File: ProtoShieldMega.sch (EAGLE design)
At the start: 32 parts, among them J1 Digital_0_7, J2 Analog, J3 Digital_8_13, J4 Analog, J5 Digital_0_7, J6 Digital_22_36, J7 Digital_23_37, J8 Digital_38_52, J9 Digital_39_53

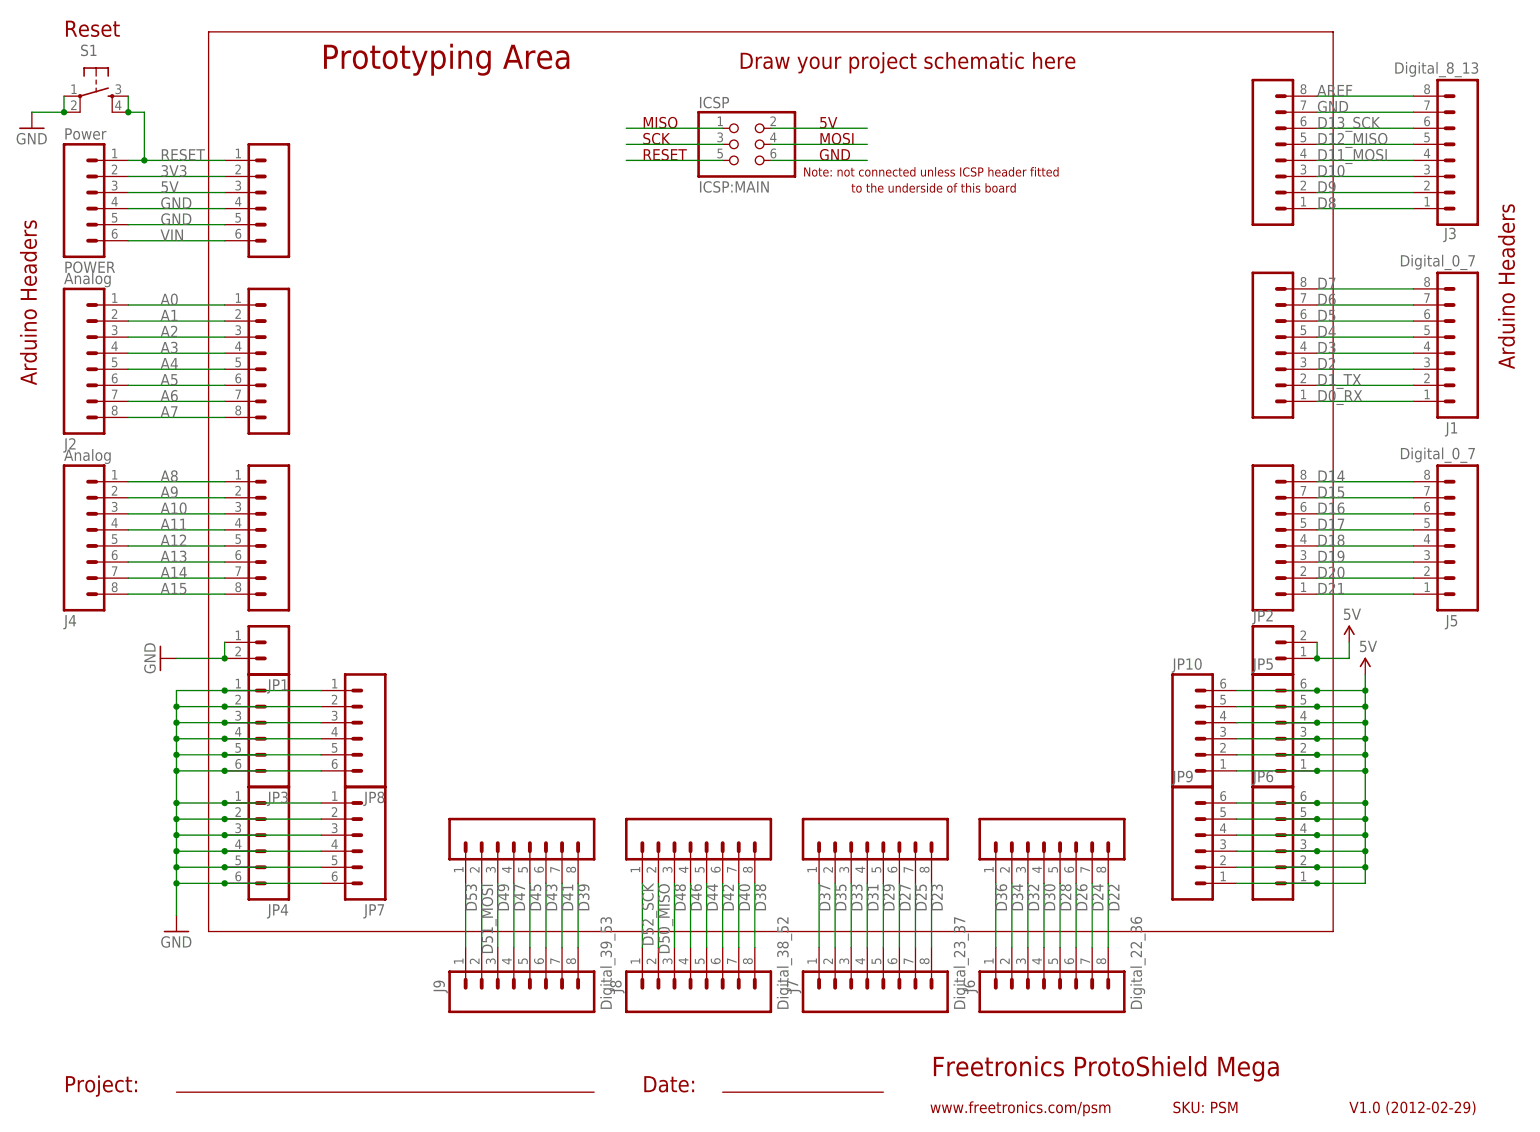
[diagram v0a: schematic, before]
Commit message: Update for Arduino R3 headers
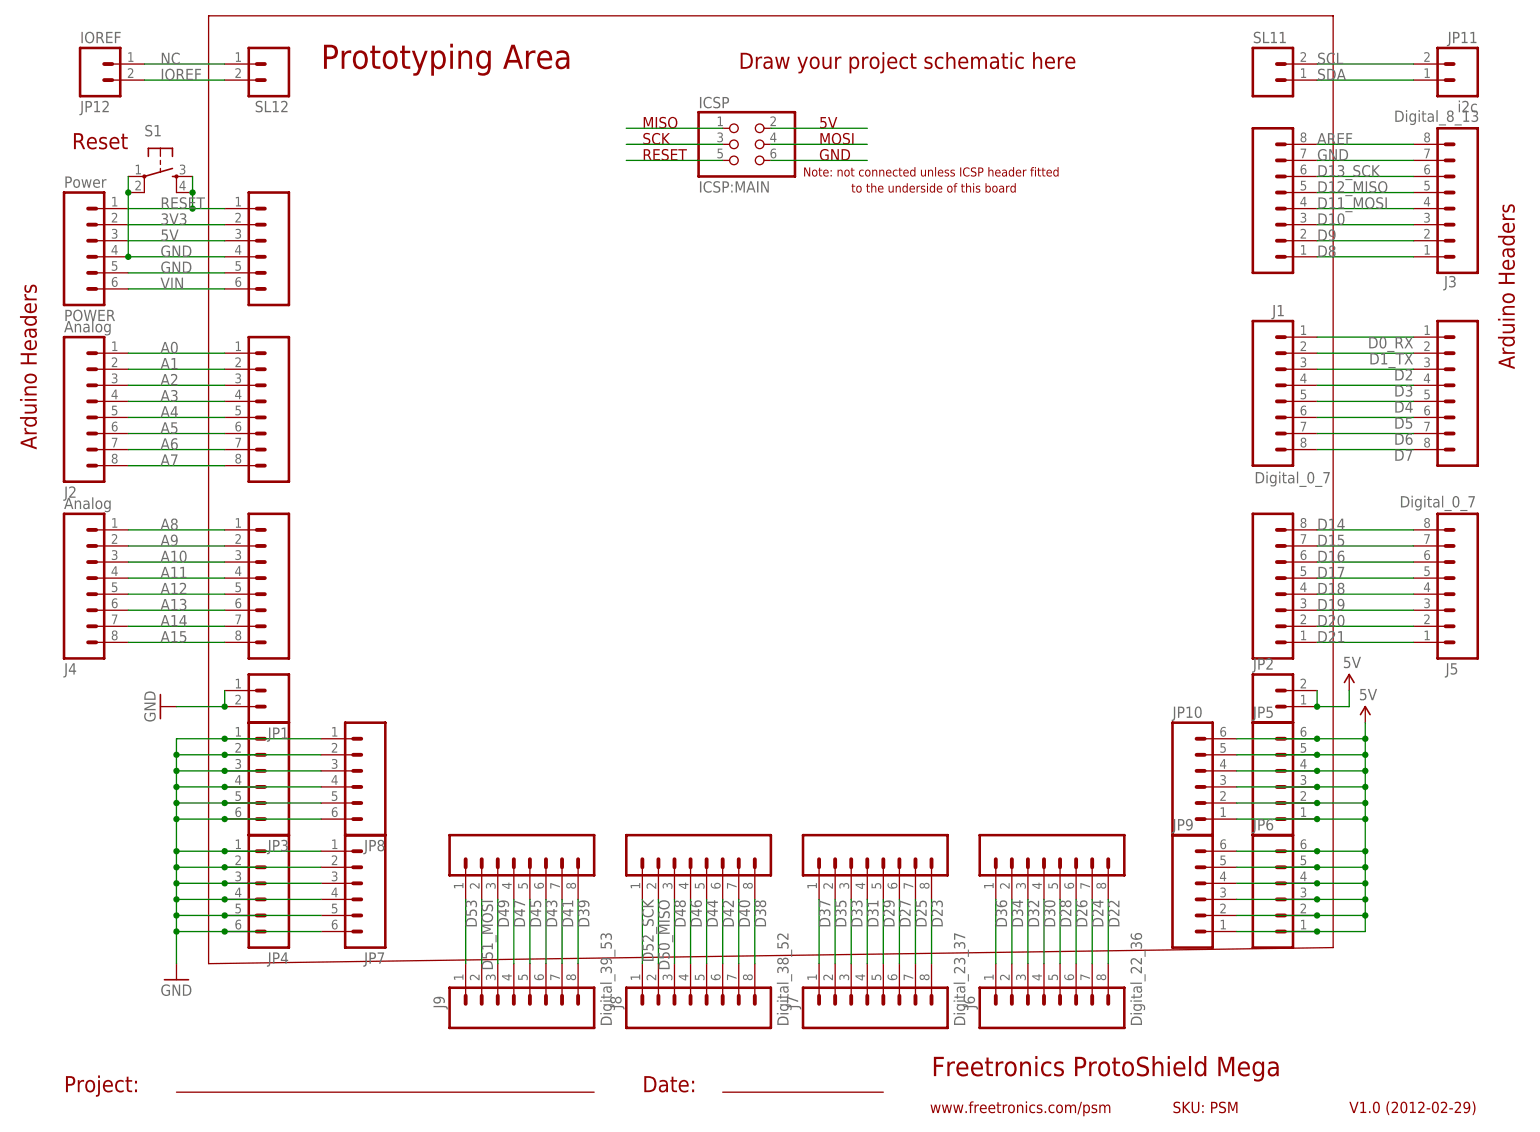
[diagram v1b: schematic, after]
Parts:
- added JP11: i2c, freetronics:M02PTH
- added JP12: IOREF, freetronics:M02PTH
- added SL11, SL12: (no value), freetronics:M02PTH
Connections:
- new net IOREF: JP12.2, SL12.2
- new net NC: JP12.1, SL12.1
- new net SCL: JP11.2, SL11.2
- new net SDA: JP11.1, SL11.1
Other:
- moved on the sheet: J1, J2, J3, J4, J5, J6, J7, J8, J9, JP1, JP10, JP2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
